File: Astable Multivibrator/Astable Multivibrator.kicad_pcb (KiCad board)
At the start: 2 copper layers, 42 x 36 mm, 13 parts, among them J1 Conn_01x02, Q1 BC547, Q2 BC547

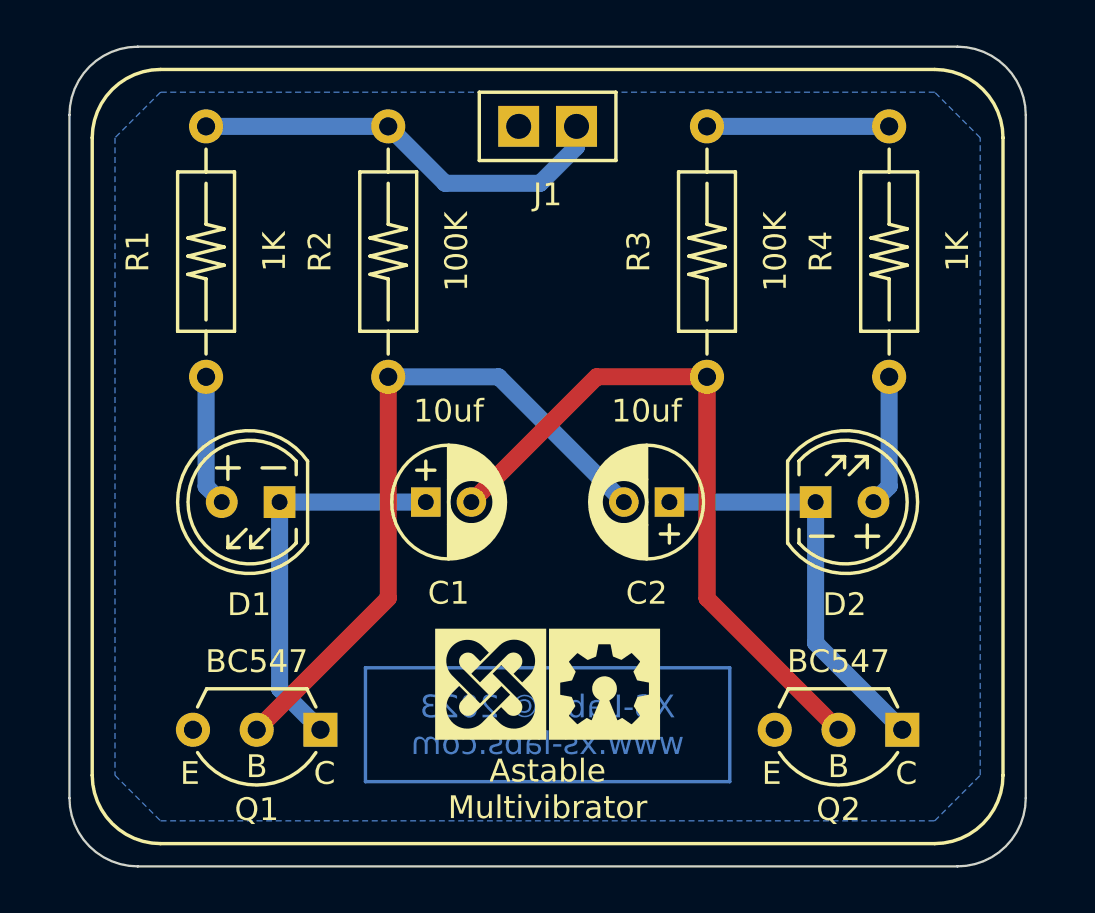
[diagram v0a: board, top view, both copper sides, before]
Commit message: feat: Replaced the pin header by a terminal block.
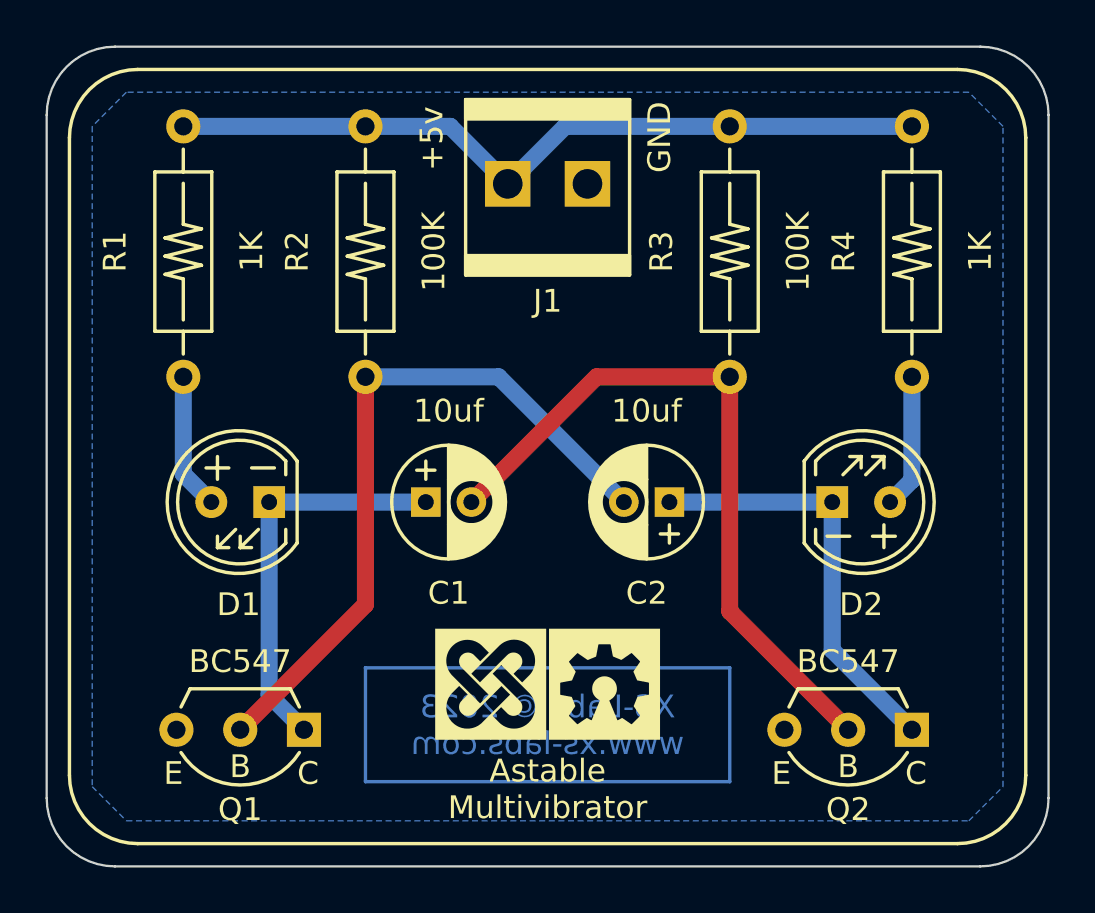
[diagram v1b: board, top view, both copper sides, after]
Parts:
- J1: footprint XS:Connector-Breakaway-Header-2.54x0.66mm-2 -> XS:Connector-Wurth-Terminal-Block-2P-3.5mm-691214110002
- moved J1 2.67 mm to (113.0, 63.2), turned to 180 degrees
- moved R1 1.00 mm to (97.0, 66.0)
- moved R2 1.00 mm to (105.0, 66.0)
- moved R3 1.00 mm to (121.0, 66.0)
- moved R4 1.00 mm to (129.0, 66.0)
- moved D2 0.73 mm to (126.8, 77.0)
- moved Q1 0.72 mm to (99.5, 87.0)
- moved D1 0.46 mm to (99.5, 77.0)
- moved Q2 0.42 mm to (126.2, 87.0)
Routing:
- net Net-(J1-Pin_2): track 26.9 -> 34.1 mm
- net Net-(Q1-B): track 30.5 -> 31.4 mm
- net Net-(Q2-B): track 30.5 -> 31.3 mm
- net Net-(D2-K): track 18.0 -> 18.6 mm
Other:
- board size 42 x 36 mm -> 44 x 36 mm
- board text added: "+5v"
- board text added: "GND"
